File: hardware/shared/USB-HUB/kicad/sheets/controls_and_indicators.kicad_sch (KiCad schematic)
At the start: 0 parts

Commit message: feat(hardware): wire 30deg optical ring power and hub USB interfaces for accessibility pointing, ~$9 ring / ~$5-6 hub BOM
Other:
- note added: "Recovery/control interface scaffold: boot, reset, UART pads, and status indication terminate on this sheet."
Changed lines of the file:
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@@
   (generator_version "0.1")
   (paper "A4")
+  (text "Recovery/control interface scaffold: boot, reset, UART pads, and status indication terminate on this sheet."
+    (at 20.32 20.32 0)
+    (effects (font (size 1.27 1.27)))
+  )
+  (hierarchical_label "EN"
+    (shape output)
+    (at 58.42 25.4 270)
+    (effects (font (size 1.27 1.27)))
+  )
+  (hierarchical_label "BOOT_N"
+    (shape output)
+    (at 66.04 25.4 270)
+    (effects (font (size 1.27 1.27)))
+  )
+  (hierarchical_label "UART_TX_DBG"
+    (shape input)
+    (at 73.66 25.4 270)
+    (effects (font (size 1.27 1.27)))
+  )
+  (hierarchical_label "UART_RX_DBG"
+    (shape output)
+    (at 81.28 25.4 270)
+    (effects (font (size 1.27 1.27)))
+  )
+  (hierarchical_label "LED_STATUS"
+    (shape input)
+    (at 88.9 25.4 270)
+    (effects (font (size 1.27 1.27)))
+  )
   (sheet_instances
     (path "/" (page "1"))

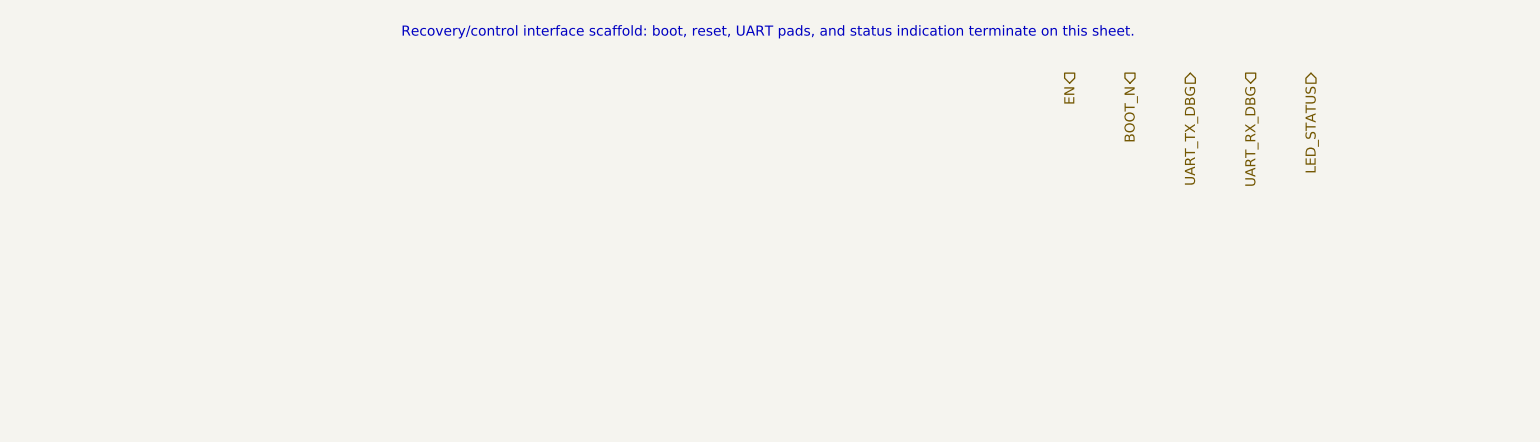
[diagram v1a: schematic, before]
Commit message: feat(usb-hub): add native usb first-board pass
Defensive publication:

- Specific sensing mechanism: no surface sensor on the hub; native USB ESP32-S3 service/programming and HID bridge capture for the PowerFinger BLE input family.

- Form factor and angle: straight inline direct-plug USB-A dongle board, first-pass 54 x 26 mm layout with reinforced SOFNG USB-05 plug retention.

- Intended use case: offline accessible first-board bring-up, repair, programming, and native-USB service for PowerFinger ring/wand development.

- BOM estimate: keeps the active USB-HUB packet inside the current ~$5-6 first-board BOM intent.

Verification:

- git diff --check -- hardware/shared/USB-HUB

- KiCad CLI ERC/DRC run locally and documented as still failing pending schematic connectivity and PCB routing closure.
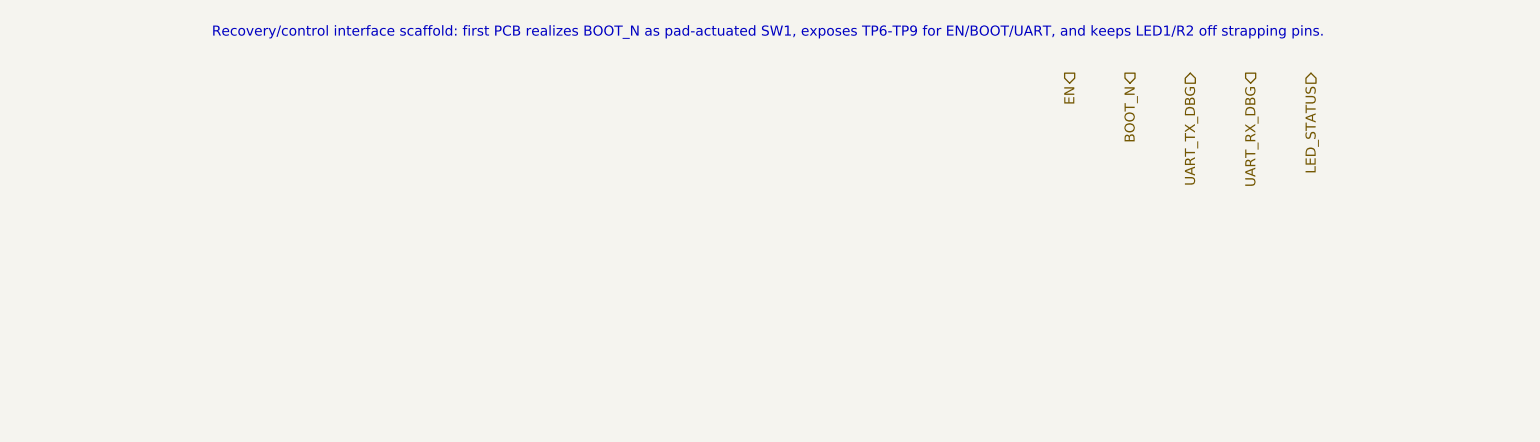
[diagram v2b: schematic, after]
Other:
- note added: "Recovery/control interface scaffold: first PCB realizes BOOT_N as pad-actuated SW1, exposes TP6-TP9 for EN/BOOT/UART, and keeps LED1/R2 off strapping pins."
- note removed: "Recovery/control interface scaffold: boot, reset, UART pads, and status indication terminate on this sheet."
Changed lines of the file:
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@@
   (generator_version "0.1")
   (paper "A4")
-  (text "Recovery/control interface scaffold: boot, reset, UART pads, and status indication terminate on this sheet."
+  (text "Recovery/control interface scaffold: first PCB realizes BOOT_N as pad-actuated SW1, exposes TP6-TP9 for EN/BOOT/UART, and keeps LED1/R2 off strapping pins."
     (at 20.32 20.32 0)
     (effects (font (size 1.27 1.27)))

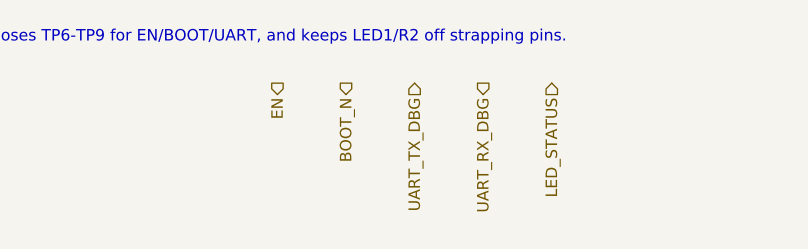
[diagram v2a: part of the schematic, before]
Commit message: feat(usb-hub): clean native USB first board pass
Sensing mechanism: none; native USB-A hub/control accessory capture for the shared USB-HUB packet.

Form factor and angle: direct-plug USB-A dongle first-board PCB; no ring angle applies.

Intended use case: offline native-USB repairable hub/control bring-up for accessibility pointing devices.

BOM estimate: kept inside the current USB-HUB approximately -6 first-board intent.
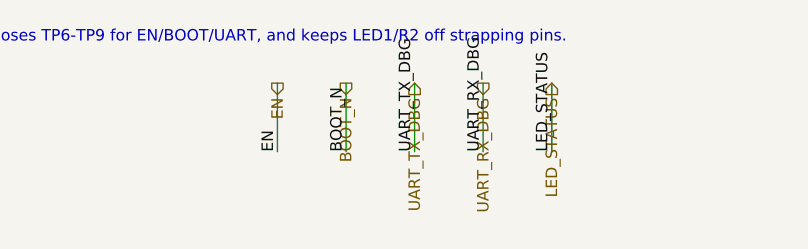
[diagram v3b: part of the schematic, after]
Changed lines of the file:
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@@
     (effects (font (size 1.27 1.27)))
+  )
+  (label "EN"
+    (at 58.42 33.02 90)
+    (effects (font (size 1.27 1.27)) (justify left bottom))
+  )
+  (label "BOOT_N"
+    (at 66.04 33.02 90)
+    (effects (font (size 1.27 1.27)) (justify left bottom))
+  )
+  (label "UART_TX_DBG"
+    (at 73.66 33.02 90)
+    (effects (font (size 1.27 1.27)) (justify left bottom))
+  )
+  (label "UART_RX_DBG"
+    (at 81.28 33.02 90)
+    (effects (font (size 1.27 1.27)) (justify left bottom))
+  )
+  (label "LED_STATUS"
+    (at 88.9 33.02 90)
+    (effects (font (size 1.27 1.27)) (justify left bottom))
+  )
+  (wire
+    (pts
+      (xy 58.42 25.4)
+      (xy 58.42 33.02)
+    )
+    (stroke (width 0) (type default) (color 0 0 0 0))
+  )
+  (wire
+    (pts
+      (xy 66.04 25.4)
+      (xy 66.04 33.02)
+    )
+    (stroke (width 0) (type default) (color 0 0 0 0))
+  )
+  (wire
+    (pts
+      (xy 73.66 25.4)
+      (xy 73.66 33.02)
+    )
+    (stroke (width 0) (type default) (color 0 0 0 0))
+  )
+  (wire
+    (pts
+      (xy 81.28 25.4)
+      (xy 81.28 33.02)
+    )
+    (stroke (width 0) (type default) (color 0 0 0 0))
+  )
+  (wire
+    (pts
+      (xy 88.9 25.4)
+      (xy 88.9 33.02)
+    )
+    (stroke (width 0) (type default) (color 0 0 0 0))
   )
   (sheet_instances

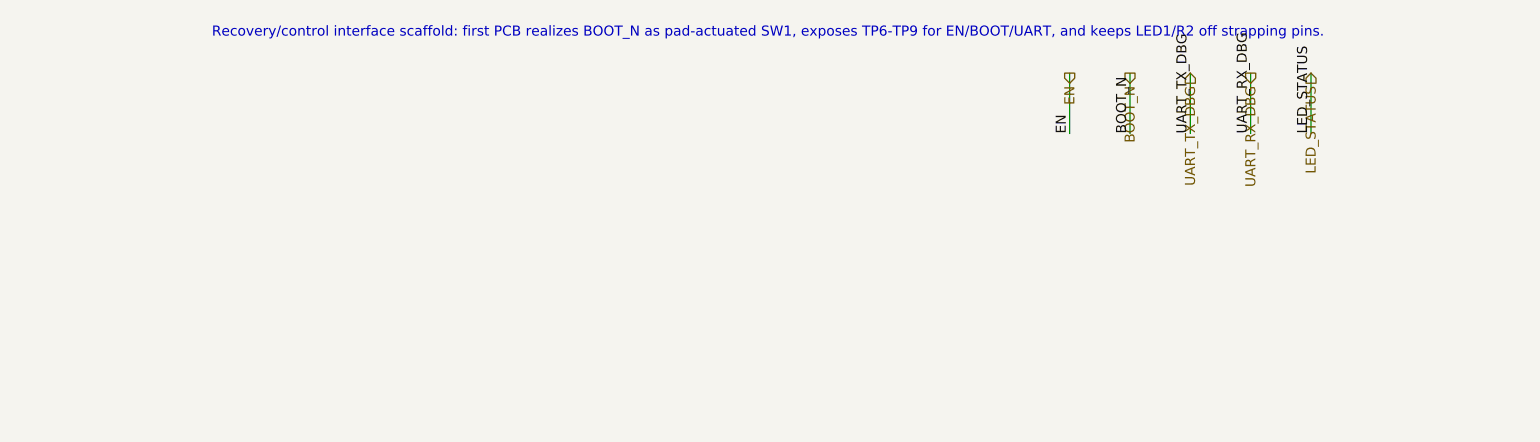
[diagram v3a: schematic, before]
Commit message: fix(usb-hub): clean native-usb dongle drc parity
Direct-plug native USB hub dongle for accessibility pointing and OCR composition; no sensing mechanism change; BOM intent remains ~-6.
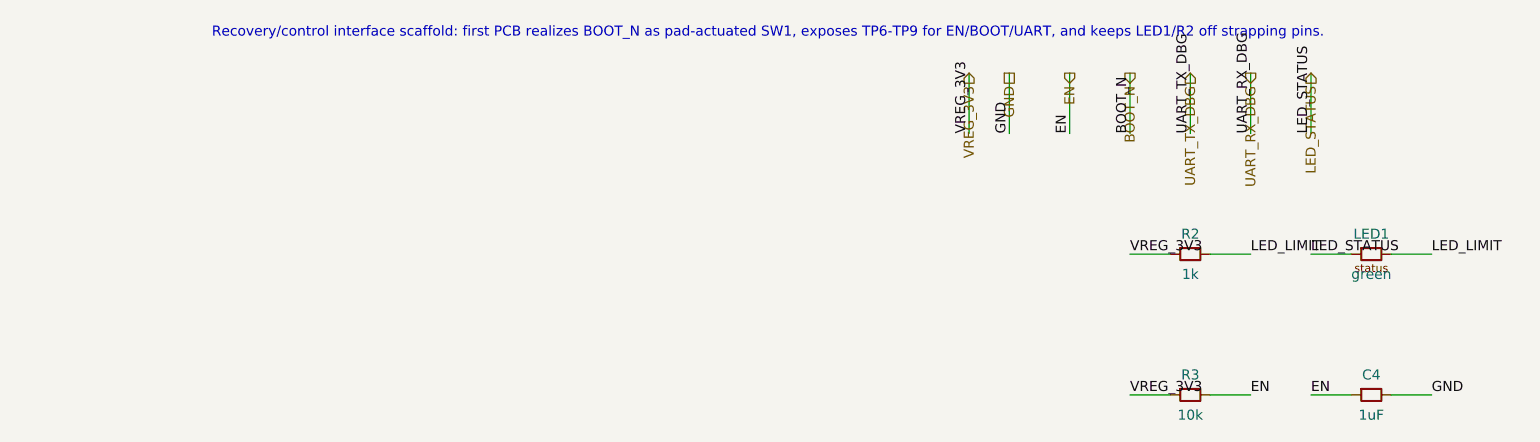
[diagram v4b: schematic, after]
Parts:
- added C4: 1uF, Capacitor_SMD:C_0402_1005Metric, symbol PowerFinger:C_0402_SUPPORT
- added LED1: green, LED_SMD:LED_0402_1005Metric, symbol PowerFinger:LED_0402_STATUS
- added R2: 1k, Resistor_SMD:R_0402_1005Metric, symbol PowerFinger:R_0402_SUPPORT
- added R3: 10k, Resistor_SMD:R_0402_1005Metric, symbol PowerFinger:R_0402_SUPPORT
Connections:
- net EN: now also C4.1, R3.2
- net LED_STATUS: now also LED1.1 (K)
- new net GND: C4.2
- new net LED_LIMIT: LED1.2 (A), R2.2
- new net VREG_3V3: R2.1, R3.1
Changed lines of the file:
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@@
     (effects (font (size 1.27 1.27)))
+  )
+  (hierarchical_label "VREG_3V3"
+    (shape input)
+    (at 45.72 25.4 270)
+    (effects (font (size 1.27 1.27)))
+  )
+  (hierarchical_label "GND"
+    (shape passive)
+    (at 50.8 25.4 270)
+    (effects (font (size 1.27 1.27)))
+  )
+  (label "VREG_3V3"
+    (at 45.72 33.02 90)
+    (effects (font (size 1.27 1.27)) (justify left bottom))
+  )
+  (label "GND"
+    (at 50.8 33.02 90)
+    (effects (font (size 1.27 1.27)) (justify left bottom))
   )
   (label "EN"
@@
     (stroke (width 0) (type default) (color 0 0 0 0))
   )
+  (wire
+    (pts
+      (xy 45.72 25.4)
+      (xy 45.72 33.02)
+    )
+    (stroke (width 0) (type default) (color 0 0 0 0))
+  )
+  (wire
+    (pts
+      (xy 50.8 25.4)
+      (xy 50.8 33.02)
+    )
+    (stroke (width 0) (type default) (color 0 0 0 0))
+  )
+  (label "VREG_3V3"
+    (at 66.04 48.26 0)
+    (effects (font (size 1.27 1.27)) (justify left bottom))
+  )
+  (label "LED_LIMIT"
+    (at 81.28 48.26 0)
+    (effects (font (size 1.27 1.27)) (justify left bottom))
+  )
+  (label "LED_STATUS"
+    (at 88.9 48.26 0)
+    (effects (font (size 1.27 1.27)) (justify left bottom))
+  )
+  (label "LED_LIMIT"
+    (at 104.14 48.26 0)
+    (effects (font (size 1.27 1.27)) (justify left bottom))
+  )
+  (label "VREG_3V3"
+    (at 66.04 66.04 0)
+    (effects (font (size 1.27 1.27)) (justify left bottom))
+  )
+  (label "EN"
+    (at 81.28 66.04 0)
+    (effects (font (size 1.27 1.27)) (justify left bottom))
+  )
+  (label "EN"
+    (at 88.9 66.04 0)
+    (effects (font (size 1.27 1.27)) (justify left bottom))
+  )
+  (label "GND"
+    (at 104.14 66.04 0)
+    (effects (font (size 1.27 1.27)) (justify left bottom))
+  )
+  (wire
+    (pts
+      (xy 66.04 48.26)
+      (xy 71.12 48.26)
+    )
+    (stroke (width 0) (type default) (color 0 0 0 0))
+  )
+  (wire
+    (pts
+      (xy 76.2 48.26)
+      (xy 81.28 48.26)
+    )
+    (stroke (width 0) (type default) (color 0 0 0 0))
+  )
+  (wire
+    (pts
+      (xy 88.9 48.26)
+      (xy 93.98 48.26)
+    )
+    (stroke (width 0) (type default) (color 0 0 0 0))
+  )
+  (wire
+    (pts
+      (xy 99.06 48.26)
+      (xy 104.14 48.26)
+    )
+    (stroke (width 0) (type default) (color 0 0 0 0))
+  )
+  (wire
+    (pts
+      (xy 66.04 66.04)
+      (xy 71.12 66.04)
+    )
+    (stroke (width 0) (type default) (color 0 0 0 0))
+  )
+  (wire
+    (pts
+      (xy 76.2 66.04)
+      (xy 81.28 66.04)
+    )
+    (stroke (width 0) (type default) (color 0 0 0 0))
+  )
+  (wire
+    (pts
+      (xy 88.9 66.04)
+      (xy 93.98 66.04)
+    )
+    (stroke (width 0) (type default) (color 0 0 0 0))
+  )
+  (wire
+    (pts
+      (xy 99.06 66.04)
+      (xy 104.14 66.04)
+    )
+    (stroke (width 0) (type default) (color 0 0 0 0))
+  )
+  (symbol (lib_id "PowerFinger:R_0402_SUPPORT") (at 73.66 48.26 0) (unit 1)
+    (in_bom yes) (on_board yes) (dnp no) (fields_autoplaced)
+    (property "Reference" "R2" (at 73.66 45.72 0)
+      (effects (font (size 1.27 1.27)))
+    )
+    (property "Value" "1k" (at 73.66 50.8 0)
+      (effects (font (size 1.27 1.27)))
+    )
+    (property "Footprint" "Resistor_SMD:R_0402_1005Metric" (at 73.66 43.18 0)
+      (effects (font (size 1.27 1.27)) hide)
+    )
+    (pin "1")
+    (pin "2")
+    (instances
+      (project "usb_hub"
+        (path "/"
+          (reference "R2") (unit 1)
+        )
+      )
+    )
+  )
+  (symbol (lib_id "PowerFinger:LED_0402_STATUS") (at 96.52 48.26 0) (unit 1)
+    (in_bom yes) (on_board yes) (dnp no) (fields_autoplaced)
+    (property "Reference" "LED1" (at 96.52 45.72 0)
+      (effects (font (size 1.27 1.27)))
+    )
+    (property "Value" "green" (at 96.52 50.8 0)
+      (effects (font (size 1.27 1.27)))
+    )
+    (property "Footprint" "LED_SMD:LED_0402_1005Metric" (at 96.52 43.18 0)
+      (effects (font (size 1.27 1.27)) hide)
+    )
+    (pin "1")
+    (pin "2")
+    (instances
+      (project "usb_hub"
+        (path "/"
+          (reference "LED1") (unit 1)
+        )
+      )
+    )
+  )
+  (symbol (lib_id "PowerFinger:R_0402_SUPPORT") (at 73.66 66.04 0) (unit 1)
+    (in_bom yes) (on_board yes) (dnp no) (fields_autoplaced)
+    (property "Reference" "R3" (at 73.66 63.5 0)
+      (effects (font (size 1.27 1.27)))
+    )
+    (property "Value" "10k" (at 73.66 68.58 0)
+      (effects (font (size 1.27 1.27)))
+    )
+    (property "Footprint" "Resistor_SMD:R_0402_1005Metric" (at 73.66 60.96 0)
+      (effects (font (size 1.27 1.27)) hide)
+    )
+    (pin "1")
+    (pin "2")
+    (instances
+      (project "usb_hub"
+        (path "/"
+          (reference "R3") (unit 1)
+        )
+      )
+    )
+  )
+  (symbol (lib_id "PowerFinger:C_0402_SUPPORT") (at 96.52 66.04 0) (unit 1)
+    (in_bom yes) (on_board yes) (dnp no) (fields_autoplaced)
+    (property "Reference" "C4" (at 96.52 63.5 0)
+      (effects (font (size 1.27 1.27)))
+    )
+    (property "Value" "1uF" (at 96.52 68.58 0)
+      (effects (font (size 1.27 1.27)))
+    )
+    (property "Footprint" "Capacitor_SMD:C_0402_1005Metric" (at 96.52 60.96 0)
+      (effects (font (size 1.27 1.27)) hide)
+    )
+    (pin "1")
+    (pin "2")
+    (instances
+      (project "usb_hub"
+        (path "/"
+          (reference "C4") (unit 1)
+        )
+      )
+    )
+  )
   (sheet_instances

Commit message: fix(usb-hub): pin local first-board footprints
Design disclosure: sensing mechanism none; form factor stepped USB-A direct-plug USB-HUB dongle; intended use offline BLE HID composition and service access for accessibility; BOM estimate ~$5-6 packet target.

Move first-board commodity/support footprints into the source-controlled PowerFinger_USB library and update the packet verification story to all-severity PCB DRC clean.
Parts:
- C4: footprint Capacitor_SMD:C_0402_1005Metric -> PowerFinger_USB:C_0402_1005Metric_FirstBoard
- LED1: footprint LED_SMD:LED_0402_1005Metric -> PowerFinger_USB:LED_0402_1005Metric_FirstBoard
- R2, R3: footprint Resistor_SMD:R_0402_1005Metric -> PowerFinger_USB:R_0402_1005Metric_FirstBoard
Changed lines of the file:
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@@
       (effects (font (size 1.27 1.27)))
     )
-    (property "Footprint" "Resistor_SMD:R_0402_1005Metric" (at 73.66 43.18 0)
+    (property "Footprint" "PowerFinger_USB:R_0402_1005Metric_FirstBoard" (at 73.66 43.18 0)
       (effects (font (size 1.27 1.27)) hide)
     )
@@
       (effects (font (size 1.27 1.27)))
     )
-    (property "Footprint" "LED_SMD:LED_0402_1005Metric" (at 96.52 43.18 0)
+    (property "Footprint" "PowerFinger_USB:LED_0402_1005Metric_FirstBoard" (at 96.52 43.18 0)
       (effects (font (size 1.27 1.27)) hide)
     )
@@
       (effects (font (size 1.27 1.27)))
     )
-    (property "Footprint" "Resistor_SMD:R_0402_1005Metric" (at 73.66 60.96 0)
+    (property "Footprint" "PowerFinger_USB:R_0402_1005Metric_FirstBoard" (at 73.66 60.96 0)
       (effects (font (size 1.27 1.27)) hide)
     )
@@
       (effects (font (size 1.27 1.27)))
     )
-    (property "Footprint" "Capacitor_SMD:C_0402_1005Metric" (at 96.52 60.96 0)
+    (property "Footprint" "PowerFinger_USB:C_0402_1005Metric_FirstBoard" (at 96.52 60.96 0)
       (effects (font (size 1.27 1.27)) hide)
     )

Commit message: fix(usb-hub): close kicad erc snapshot
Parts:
- added TP6: EN, PowerFinger_USB:TestPoint_Pad_D1.0mm_FirstBoard, symbol PowerFinger:SERVICE_PAD
- added TP7: BOOT, PowerFinger_USB:TestPoint_Pad_D1.0mm_FirstBoard, symbol PowerFinger:SERVICE_PAD
- added TP8: TX, PowerFinger_USB:TestPoint_Pad_D1.0mm_FirstBoard, symbol PowerFinger:SERVICE_PAD
- added TP9: RX, PowerFinger_USB:TestPoint_Pad_D1.0mm_FirstBoard, symbol PowerFinger:SERVICE_PAD
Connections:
- net BOOT_N: now also TP7.1
- net EN: now also TP6.1
- net UART_RX_DBG: now also TP9.1
- net UART_TX_DBG: now also TP8.1
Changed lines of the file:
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@@
+    )
+  )
+  (symbol (lib_id "PowerFinger:SERVICE_PAD") (at 60.96 33.02 0) (unit 1)
+    (in_bom no) (on_board yes) (dnp no)
+    (property "Reference" "TP6" (at 60.96 30.48 0)
+      (effects (font (size 1.27 1.27)))
+    )
+    (property "Value" "EN" (at 60.96 35.56 0)
+      (effects (font (size 1.27 1.27)))
+    )
+    (property "Footprint" "PowerFinger_USB:TestPoint_Pad_D1.0mm_FirstBoard" (at 60.96 27.94 0)
+      (effects (font (size 1.27 1.27)) hide)
+    )
+    (pin "1")
+    (instances
+      (project "usb_hub"
+        (path "/"
+          (reference "TP6") (unit 1)
+        )
+      )
+    )
+  )
+  (symbol (lib_id "PowerFinger:SERVICE_PAD") (at 68.58 33.02 0) (unit 1)
+    (in_bom no) (on_board yes) (dnp no)
+    (property "Reference" "TP7" (at 68.58 30.48 0)
+      (effects (font (size 1.27 1.27)))
+    )
+    (property "Value" "BOOT" (at 68.58 35.56 0)
+      (effects (font (size 1.27 1.27)))
+    )
+    (property "Footprint" "PowerFinger_USB:TestPoint_Pad_D1.0mm_FirstBoard" (at 68.58 27.94 0)
+      (effects (font (size 1.27 1.27)) hide)
+    )
+    (pin "1")
+    (instances
+      (project "usb_hub"
+        (path "/"
+          (reference "TP7") (unit 1)
+        )
+      )
+    )
+  )
+  (symbol (lib_id "PowerFinger:SERVICE_PAD") (at 76.2 33.02 0) (unit 1)
+    (in_bom no) (on_board yes) (dnp no)
+    (property "Reference" "TP8" (at 76.2 30.48 0)
+      (effects (font (size 1.27 1.27)))
+    )
+    (property "Value" "TX" (at 76.2 35.56 0)
+      (effects (font (size 1.27 1.27)))
+    )
+    (property "Footprint" "PowerFinger_USB:TestPoint_Pad_D1.0mm_FirstBoard" (at 76.2 27.94 0)
+      (effects (font (size 1.27 1.27)) hide)
+    )
+    (pin "1")
+    (instances
+      (project "usb_hub"
+        (path "/"
+          (reference "TP8") (unit 1)
+        )
+      )
+    )
+  )
+  (symbol (lib_id "PowerFinger:SERVICE_PAD") (at 83.82 33.02 0) (unit 1)
+    (in_bom no) (on_board yes) (dnp no)
+    (property "Reference" "TP9" (at 83.82 30.48 0)
+      (effects (font (size 1.27 1.27)))
+    )
+    (property "Value" "RX" (at 83.82 35.56 0)
+      (effects (font (size 1.27 1.27)))
+    )
+    (property "Footprint" "PowerFinger_USB:TestPoint_Pad_D1.0mm_FirstBoard" (at 83.82 27.94 0)
+      (effects (font (size 1.27 1.27)) hide)
+    )
+    (pin "1")
+    (instances
+      (project "usb_hub"
+        (path "/"
+          (reference "TP9") (unit 1)
+        )
+      )
     )
   )
